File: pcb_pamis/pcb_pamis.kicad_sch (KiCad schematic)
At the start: 39 parts, among them J1 USB_C_Receptacle_USB2.0_16P, J10 Conn_01x03, J11 Conn_01x03, J12 Conn_02x06_Odd_Even, J2 1755736, J6 Conn_01x05, J7 Conn_01x05, J8 Conn_01x05, J9 Conn_01x03, Q1 Q_NPN_BEC, Q2 Q_NPN_BEC, SW1 SW_Push, U1 ESP32-WROOM-32UE, U2 CP2102N-Axx-xQFN28

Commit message: ajout fixations
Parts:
- added H1, H2, H3, H4: MountingHole_Pad, MountingHole:MountingHole_3.2mm_M3_ISO14580_Pad_TopBottom, symbol Mechanical:MountingHole_Pad
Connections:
- net GND: now also H1.1, H2.1, H3.1, H4.1

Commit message: commencement correctifs PCB Pami
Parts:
- H1, H2, H3, H4: footprint MountingHole:MountingHole_3.2mm_M3_ISO14580_Pad_TopBottom -> MountingHole:MountingHole_3.2mm_M3_Pad
- J10, J11, J9: footprint Connector_PinHeader_1.27mm:PinHeader_1x03_P1.27mm_Vertical -> Connector_PinHeader_2.54mm:PinHeader_1x03_P2.54mm_Vertical
- J12: footprint Connector_PinHeader_1.27mm:PinHeader_2x06_P1.27mm_Vertical -> Connector_PinHeader_2.54mm:PinHeader_2x06_P2.54mm_Vertical
- J6, J7, J8: footprint Connector_PinHeader_1.27mm:PinHeader_1x05_P1.27mm_Vertical -> Connector_PinHeader_2.54mm:PinHeader_1x05_P2.54mm_Vertical
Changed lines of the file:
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@@
 			)
 		)
-		(property "Footprint" "Connector_PinHeader_1.27mm:PinHeader_2x06_P1.27mm_Vertical"
+		(property "Footprint" "Connector_PinHeader_2.54mm:PinHeader_2x06_P2.54mm_Vertical"
 			(at 71.12 181.61 0)
 			(effects
@@
 			)
 		)
-		(property "Footprint" "Connector_PinHeader_1.27mm:PinHeader_1x03_P1.27mm_Vertical"
+		(property "Footprint" "Connector_PinHeader_2.54mm:PinHeader_1x03_P2.54mm_Vertical"
 			(at 100.33 80.01 0)
 			(effects
@@
 			)
 		)
-		(property "Footprint" "MountingHole:MountingHole_3.2mm_M3_ISO14580_Pad_TopBottom"
+		(property "Footprint" "MountingHole:MountingHole_3.2mm_M3_Pad"
 			(at 125.73 147.32 0)
 			(effects
@@
 			)
 		)
-		(property "Footprint" "Connector_PinHeader_1.27mm:PinHeader_1x05_P1.27mm_Vertical"
+		(property "Footprint" "Connector_PinHeader_2.54mm:PinHeader_1x05_P2.54mm_Vertical"
 			(at 81.28 111.76 0)
 			(effects
@@
 			)
 		)
-		(property "Footprint" "Connector_PinHeader_1.27mm:PinHeader_1x03_P1.27mm_Vertical"
+		(property "Footprint" "Connector_PinHeader_2.54mm:PinHeader_1x03_P2.54mm_Vertical"
 			(at 76.2 80.01 0)
 			(effects
@@
 			)
 		)
-		(property "Footprint" "Connector_PinHeader_1.27mm:PinHeader_1x03_P1.27mm_Vertical"
+		(property "Footprint" "Connector_PinHeader_2.54mm:PinHeader_1x03_P2.54mm_Vertical"
 			(at 125.73 80.01 0)
 			(effects
@@
 			)
 		)
-		(property "Footprint" "Connector_PinHeader_1.27mm:PinHeader_1x05_P1.27mm_Vertical"
+		(property "Footprint" "Connector_PinHeader_2.54mm:PinHeader_1x05_P2.54mm_Vertical"
 			(at 81.28 147.32 0)
 			(effects
@@
 			)
 		)
-		(property "Footprint" "MountingHole:MountingHole_3.2mm_M3_ISO14580_Pad_TopBottom"
+		(property "Footprint" "MountingHole:MountingHole_3.2mm_M3_Pad"
 			(at 140.97 147.32 0)
 			(effects
@@
 			)
 		)
-		(property "Footprint" "MountingHole:MountingHole_3.2mm_M3_ISO14580_Pad_TopBottom"
+		(property "Footprint" "MountingHole:MountingHole_3.2mm_M3_Pad"
 			(at 118.11 147.32 0)
 			(effects
@@
 			)
 		)
-		(property "Footprint" "MountingHole:MountingHole_3.2mm_M3_ISO14580_Pad_TopBottom"
+		(property "Footprint" "MountingHole:MountingHole_3.2mm_M3_Pad"
 			(at 133.35 147.32 0)
 			(effects
@@
 			)
 		)
-		(property "Footprint" "Connector_PinHeader_1.27mm:PinHeader_1x05_P1.27mm_Vertical"
+		(property "Footprint" "Connector_PinHeader_2.54mm:PinHeader_1x05_P2.54mm_Vertical"
 			(at 81.28 129.54 0)
 			(effects

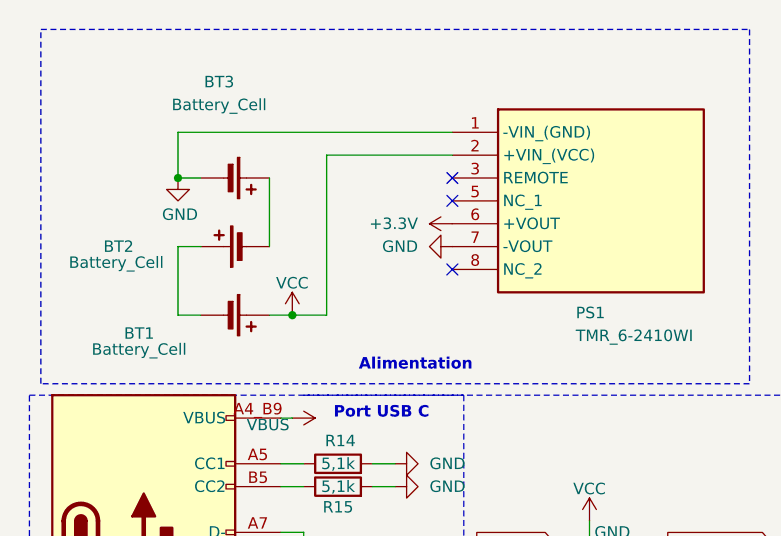
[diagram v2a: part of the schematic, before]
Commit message: finalisation nouveau routage
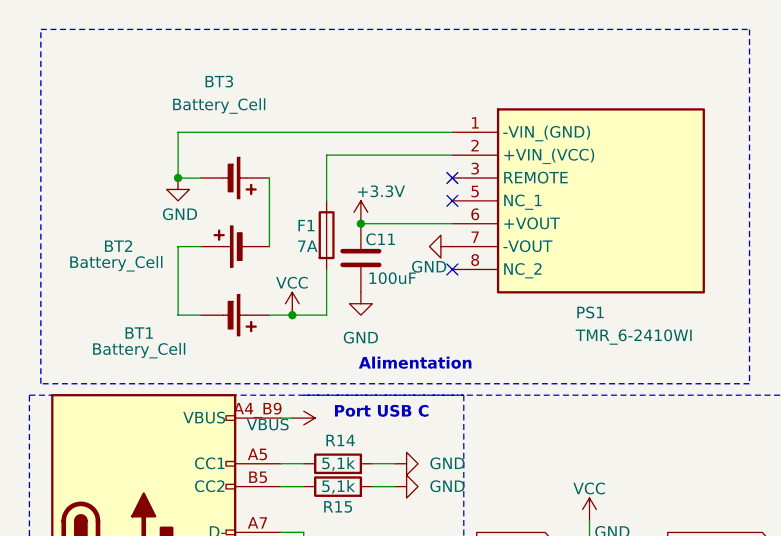
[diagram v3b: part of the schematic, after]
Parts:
- added C11: 100uF, Capacitor_SMD:C_1206_3216Metric_Pad1.33x1.80mm_HandSolder, symbol Device:C
- added F1: 7A, Modelec:01550900M, symbol Device:Fuse
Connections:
- net +3.3V: now also C11.1
- net GND: now also C11.2
- net VCC: now also F1.2; no longer PS1.2 (+VIN_(VCC))
- new net: F1.1, PS1.2 (+VIN_(VCC))
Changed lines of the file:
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@@
 	)
 	(junction
+		(at 50.8 35.56)
+		(diameter 0)
+		(color 0 0 0 0)
+	)
+	(junction
 		(at 182.88 149.86)
 		(diameter 0)
@@
 	(wire
 		(pts
-			(xy 265.43 19.05) (xy 265.43 22.86)
+			(xy 46.99 27.94) (xy 46.99 33.02)
 		)
 		(stroke
@@
 	(wire
 		(pts
-			(xy 165.1 33.02) (xy 163.83 33.02)
+			(xy 265.43 19.05) (xy 265.43 22.86)
 		)
 		(stroke
@@
 	(wire
 		(pts
-			(xy 46.99 45.72) (xy 46.99 27.94)
+			(xy 165.1 33.02) (xy 163.83 33.02)
 		)
 		(stroke
@@
 	(wire
 		(pts
+			(xy 50.8 35.56) (xy 60.96 35.56)
+		)
+		(stroke
+			(width 0)
+			(type default)
+		)
+	)
+	(wire
+		(pts
 			(xy 236.22 114.3) (xy 237.49 114.3)
 		)
@@
 		)
 	)
+	(wire
+		(pts
+			(xy 46.99 40.64) (xy 46.99 45.72)
+		)
+		(stroke
+			(width 0)
+			(type default)
+		)
+	)
 	(polyline
 		(pts
@@
 	(symbol
 		(lib_id "power:GND")
+		(at 50.8 43.18 0)
+		(unit 1)
+		(exclude_from_sim no)
+		(in_bom yes)
+		(on_board yes)
+		(dnp no)
+		(fields_autoplaced yes)
+		(property "Reference" "#PWR070"
+			(at 50.8 49.53 0)
+			(effects
+				(font
+					(size 1.27 1.27)
+				)
+				(hide yes)
+			)
+		)
+		(property "Value" "GND"
+			(at 50.8 48.26 0)
+			(effects
+				(font
+					(size 1.27 1.27)
+				)
+			)
+		)
+		(property "Footprint" ""
+			(at 50.8 43.18 0)
+			(effects
+				(font
+					(size 1.27 1.27)
+				)
+				(hide yes)
+			)
+		)
+		(property "Datasheet" ""
+			(at 50.8 43.18 0)
+			(effects
+				(font
+					(size 1.27 1.27)
+				)
+				(hide yes)
+			)
+		)
+		(property "Description" "Power symbol creates a global label with name \"GND\" , ground"
+			(at 50.8 43.18 0)
+			(effects
+				(font
+					(size 1.27 1.27)
+				)
+				(hide yes)
+			)
+		)
+		(pin "1"
+		)
+		(instances
+			(project ""
+				(path "/cd04cd30-6b87-4bc2-a277-438dac0065f3"
+					(reference "#PWR070")
+					(unit 1)
+				)
+			)
+		)
+	)
+	(symbol
+		(lib_id "power:GND")
 		(at 78.74 176.53 90)
 		(unit 1)
@@
 		(on_board yes)
 		(dnp no)
-		(fields_autoplaced yes)
 		(property "Reference" "#PWR02"
 			(at 54.61 38.1 0)
@@
 		)
 		(property "Value" "GND"
-			(at 57.15 38.0999 90)
+			(at 56.388 40.386 90)
 			(effects
 				(font
 					(size 1.27 1.27)
 				)
-				(justify right)
+				(justify left)
 			)
 		)
@@
 	)
 	(symbol
+		(lib_id "Device:Fuse")
+		(at 46.99 36.83 0)
+		(unit 1)
+		(exclude_from_sim no)
+		(in_bom yes)
+		(on_board yes)
+		(dnp no)
+		(property "Reference" "F1"
+			(at 43.688 35.814 0)
+			(effects
+				(font
+					(size 1.27 1.27)
+				)
+				(justify left)
+			)
+		)
+		(property "Value" "7A"
+			(at 43.688 38.1 0)
+			(effects
+				(font
+					(size 1.27 1.27)
+				)
+				(justify left)
+			)
+		)
+		(property "Footprint" "Modelec:01550900M"
+			(at 45.212 36.83 90)
+			(effects
+				(font
+					(size 1.27 1.27)
+				)
+				(hide yes)
+			)
+		)
+		(property "Datasheet" "~"
+			(at 46.99 36.83 0)
+			(effects
+				(font
+					(size 1.27 1.27)
+				)
+				(hide yes)
+			)
+		)
+		(property "Description" "Fuse"
+			(at 46.99 36.83 0)
+			(effects
+				(font
+					(size 1.27 1.27)
+				)
+				(hide yes)
+			)
+		)
+		(pin "2"
+		)
+		(pin "1"
+		)
+		(instances
+			(project ""
+				(path "/cd04cd30-6b87-4bc2-a277-438dac0065f3"
+					(reference "F1")
+					(unit 1)
+				)
+			)
+		)
+	)
+	(symbol
 		(lib_id "power:+3.3V")
 		(at 76.2 124.46 90)
@@
 	)
 	(symbol
+		(lib_id "Device:C")
+		(at 50.8 39.37 0)
+		(unit 1)
+		(exclude_from_sim no)
+		(in_bom yes)
+		(on_board yes)
+		(dnp no)
+		(property "Reference" "C11"
+			(at 51.308 37.338 0)
+			(effects
+				(font
+					(size 1.27 1.27)
+				)
+				(justify left)
+			)
+		)
+		(property "Value" "100uF"
+			(at 51.562 41.656 0)
+			(effects
+				(font
+					(size 1.27 1.27)
+				)
+				(justify left)
+			)
+		)
+		(property "Footprint" "Capacitor_SMD:C_1206_3216Metric_Pad1.33x1.80mm_HandSolder"
+			(at 51.7652 43.18 0)
+			(effects
+				(font
+					(size 1.27 1.27)
+				)
+				(hide yes)
+			)
+		)
+		(property "Datasheet" "~"
+			(at 50.8 39.37 0)
+			(effects
+				(font
+					(size 1.27 1.27)
+				)
+				(hide yes)
+			)
+		)
+		(property "Description" "Unpolarized capacitor"
+			(at 50.8 39.37 0)
+			(effects
+				(font
+					(size 1.27 1.27)
+				)
+				(hide yes)
+			)
+		)
+		(pin "2"
+		)
+		(pin "1"
+		)
+		(instances
+			(project ""
+				(path "/cd04cd30-6b87-4bc2-a277-438dac0065f3"
+					(reference "C11")
+					(unit 1)
+				)
+			)
+		)
+	)
+	(symbol
 		(lib_id "power:GND")
 		(at 128.27 74.93 180)
@@
 	(symbol
 		(lib_id "power:+3.3V")
-		(at 60.96 35.56 90)
+		(at 50.8 35.56 0)
 		(unit 1)
 		(exclude_from_sim no)
@@
 		(on_board yes)
 		(dnp no)
-		(fields_autoplaced yes)
 		(property "Reference" "#PWR01"
-			(at 64.77 35.56 0)
+			(at 50.8 39.37 0)
 			(effects
 				(font
@@
 		)
 		(property "Value" "+3.3V"
-			(at 57.15 35.5599 90)
+			(at 50.292 32.004 0)
 			(effects
 				(font
@@
 		)
 		(property "Footprint" ""
-			(at 60.96 35.56 0)
+			(at 50.8 35.56 0)
 			(effects
 				(font
@@
 		)
 		(property "Datasheet" ""
-			(at 60.96 35.56 0)
+			(at 50.8 35.56 0)
 			(effects
 				(font
@@
 		)
 		(property "Description" "Power symbol creates a global label with name \"+3.3V\""
-			(at 60.96 35.56 0)
+			(at 50.8 35.56 0)
 			(effects
 				(font

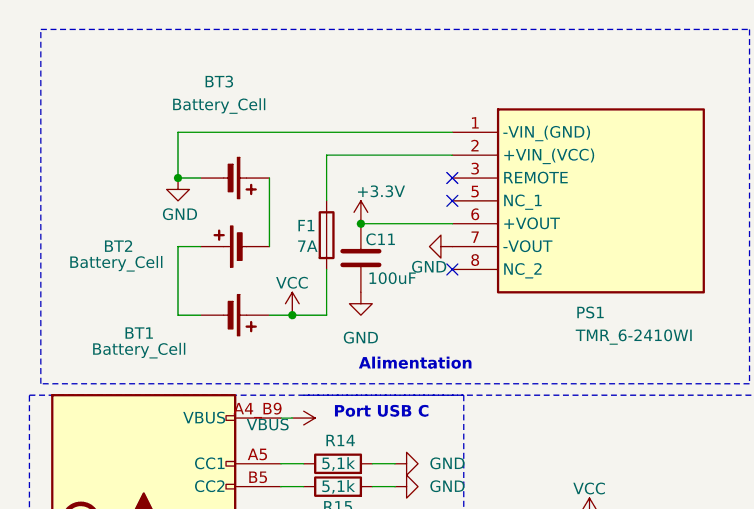
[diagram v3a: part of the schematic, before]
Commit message: déplacement fusible
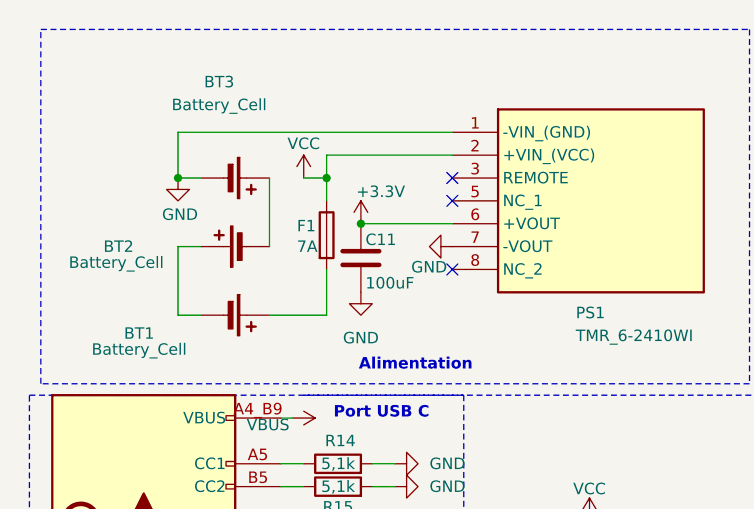
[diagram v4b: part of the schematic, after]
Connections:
- net VCC: now also F1.1, PS1.2 (+VIN_(VCC)); no longer BT1.P (+), F1.2
- new net: BT1.P (+), F1.2
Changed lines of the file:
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@@
 	)
 	(junction
-		(at 43.18 45.72)
-		(diameter 0)
-		(color 0 0 0 0)
-	)
-	(junction
 		(at 200.66 154.94)
 		(diameter 0)
@@
 	)
 	(junction
+		(at 46.99 30.48)
+		(diameter 0)
+		(color 0 0 0 0)
+	)
+	(junction
 		(at 25.4 120.65)
 		(diameter 0)
@@
 	(wire
 		(pts
+			(xy 44.45 30.48) (xy 46.99 30.48)
+		)
+		(stroke
+			(width 0)
+			(type default)
+		)
+	)
+	(wire
+		(pts
 			(xy 154.94 33.02) (xy 154.94 43.18)
 		)
@@
 	(wire
 		(pts
-			(xy 46.99 27.94) (xy 46.99 33.02)
+			(xy 46.99 30.48) (xy 46.99 33.02)
+		)
+		(stroke
+			(width 0)
+			(type default)
+		)
+	)
+	(wire
+		(pts
+			(xy 46.99 27.94) (xy 46.99 30.48)
 		)
 		(stroke
@@
 	(wire
 		(pts
-			(xy 43.18 45.72) (xy 40.64 45.72)
+			(xy 40.64 45.72) (xy 46.99 45.72)
 		)
 		(stroke
@@
 	(wire
 		(pts
-			(xy 43.18 45.72) (xy 46.99 45.72)
-		)
-		(stroke
-			(width 0)
-			(type default)
-		)
-	)
-	(wire
-		(pts
 			(xy 170.18 76.2) (xy 172.72 76.2)
 		)
@@
 	)
 	(symbol
-		(lib_id "power:VCC")
-		(at 43.18 45.72 0)
-		(unit 1)
-		(exclude_from_sim no)
-		(in_bom yes)
-		(on_board yes)
-		(dnp no)
-		(property "Reference" "#PWR032"
-			(at 43.18 49.53 0)
-			(effects
-				(font
-					(size 1.27 1.27)
-				)
-				(hide yes)
-			)
-		)
-		(property "Value" "VCC"
-			(at 43.18 42.164 0)
-			(effects
-				(font
-					(size 1.27 1.27)
-				)
-			)
-		)
-		(property "Footprint" ""
-			(at 43.18 45.72 0)
-			(effects
-				(font
-					(size 1.27 1.27)
-				)
-				(hide yes)
-			)
-		)
-		(property "Datasheet" ""
-			(at 43.18 45.72 0)
-			(effects
-				(font
-					(size 1.27 1.27)
-				)
-				(hide yes)
-			)
-		)
-		(property "Description" "Power symbol creates a global label with name \"VCC\""
-			(at 43.18 45.72 0)
-			(effects
-				(font
-					(size 1.27 1.27)
-				)
-				(hide yes)
-			)
-		)
-		(pin "1"
-		)
-		(instances
-			(project "pcb_pamis"
-				(path "/cd04cd30-6b87-4bc2-a277-438dac0065f3"
-					(reference "#PWR032")
-					(unit 1)
-				)
-			)
-		)
-	)
-	(symbol
 		(lib_id "power:GND")
 		(at 20.32 160.02 0)
@@
 	)
 	(symbol
+		(lib_id "power:VCC")
+		(at 44.45 30.48 0)
+		(unit 1)
+		(exclude_from_sim no)
+		(in_bom yes)
+		(on_board yes)
+		(dnp no)
+		(property "Reference" "#PWR032"
+			(at 44.45 34.29 0)
+			(effects
+				(font
+					(size 1.27 1.27)
+				)
+				(hide yes)
+			)
+		)
+		(property "Value" "VCC"
+			(at 44.45 26.67 0)
+			(effects
+				(font
+					(size 1.27 1.27)
+				)
+			)
+		)
+		(property "Footprint" ""
+			(at 44.45 30.48 0)
+			(effects
+				(font
+					(size 1.27 1.27)
+				)
+				(hide yes)
+			)
+		)
+		(property "Datasheet" ""
+			(at 44.45 30.48 0)
+			(effects
+				(font
+					(size 1.27 1.27)
+				)
+				(hide yes)
+			)
+		)
+		(property "Description" "Power symbol creates a global label with name \"VCC\""
+			(at 44.45 30.48 0)
+			(effects
+				(font
+					(size 1.27 1.27)
+				)
+				(hide yes)
+			)
+		)
+		(pin "1"
+		)
+		(instances
+			(project ""
+				(path "/cd04cd30-6b87-4bc2-a277-438dac0065f3"
+					(reference "#PWR032")
+					(unit 1)
+				)
+			)
+		)
+	)
+	(symbol
 		(lib_id "power:+3.3V")
 		(at 186.69 114.3 180)
@@
 		)
 		(property "Value" "100uF"
-			(at 51.562 41.656 0)
+			(at 51.308 42.164 0)
 			(effects
 				(font

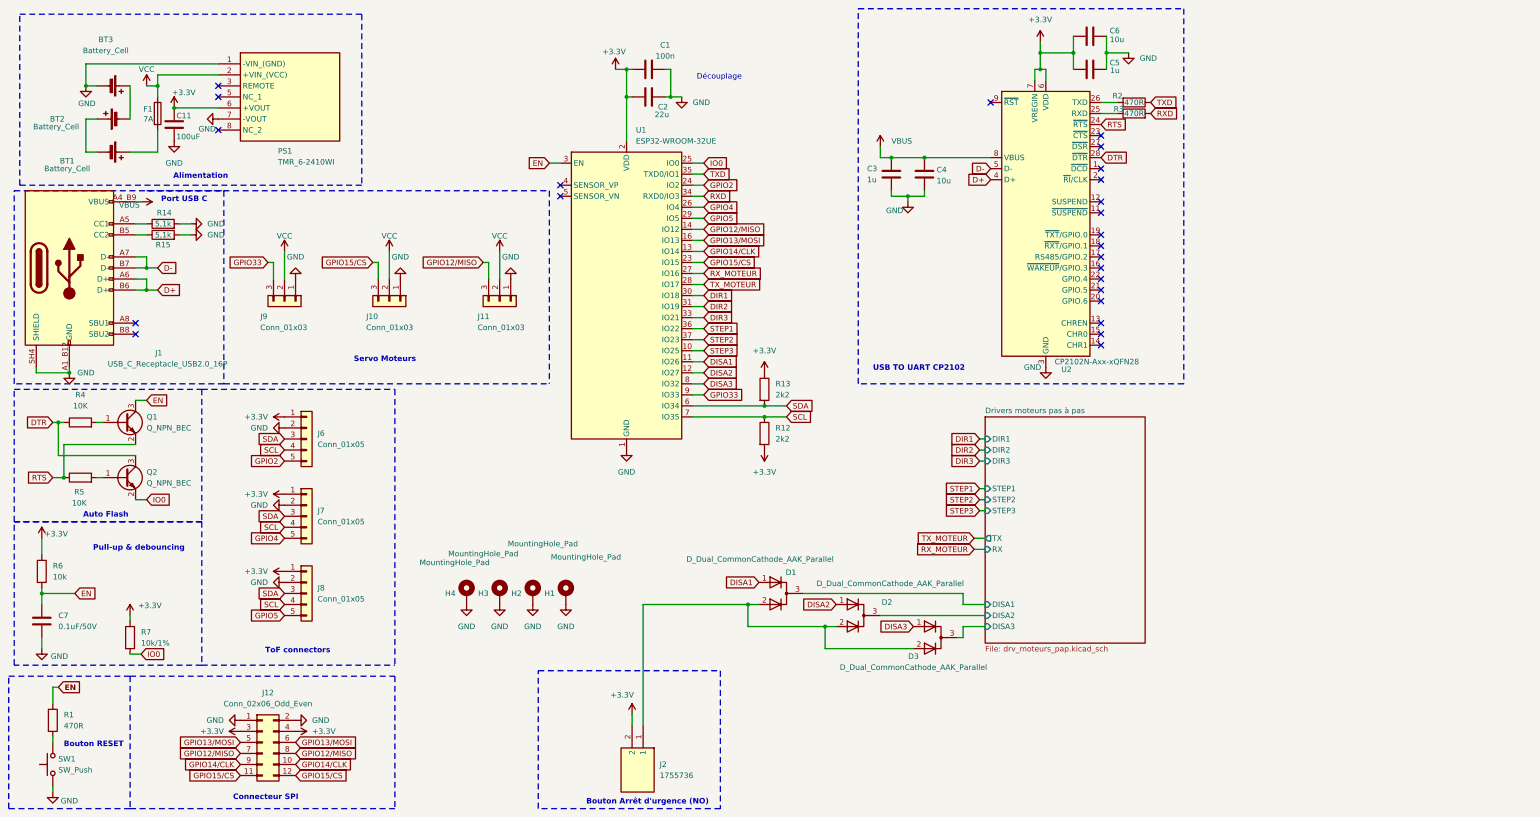
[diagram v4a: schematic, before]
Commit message: Ajout BAU servo PAMI, finitions PCB Actionneurs, fichier fab stencil. Version commandée PAMI & Actionneurs
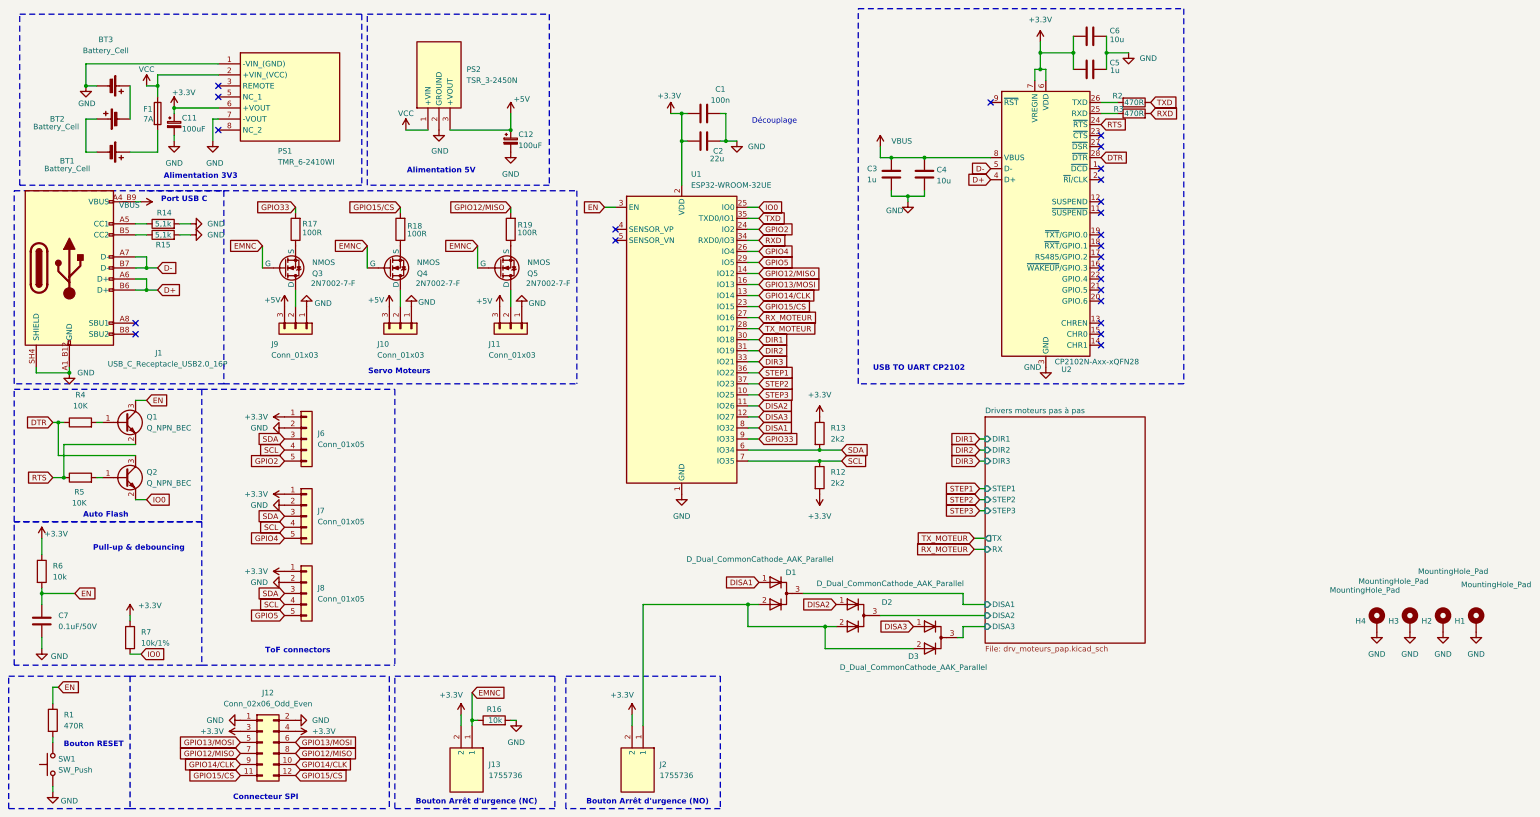
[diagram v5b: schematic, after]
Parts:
- removed C11: 100uF, Capacitor_SMD:C_1206_3216Metric_Pad1.33x1.80mm_HandSolder, symbol Device:C
- added C11, C12: 100uF, Capacitor_THT:C_Radial_D6.3mm_H11.0mm_P2.50mm, symbol Device:C_Polarized_Small
- added J13: 1755736, Modelec:PhoenixContact_MSTBVA_2,5_2-G-5,08_1x02_P5.08mm_Vertical, symbol Modelec:1755736
- added PS2: TSR_3-2450N, Modelec:TSR32450N, symbol Modelec:TSR_3-2450N
- added Q3, Q4, Q5: NMOS, Package_TO_SOT_SMD:SOT-23, symbol Simulation_SPICE:NMOS
- added R16: 10k, Resistor_SMD:R_0805_2012Metric_Pad1.20x1.40mm_HandSolder, symbol Device:R
- added R17, R18, R19: 100R, Resistor_SMD:R_0805_2012Metric_Pad1.20x1.40mm_HandSolder, symbol Device:R
- C2: footprint Capacitor_SMD:C_0805_2012Metric_Pad1.18x1.45mm_HandSolder -> Capacitor_SMD:C_1206_3216Metric_Pad1.33x1.80mm_HandSolder
- PS1: footprint TMR60510 -> Modelec:TMR60510
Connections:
- net +3.3V: now also C11.1, J13.2
- net DISA1: now also U1.8 (IO32); no longer U1.11 (IO26)
- net DISA2: now also U1.11 (IO26); no longer U1.12 (IO27)
- net DISA3: now also U1.12 (IO27); no longer U1.8 (IO32)
- net GND: now also C11.2, C12.2, PS2.2 (GROUND), R16.2
- net GPIO12/MISO: now also R19.2; no longer J11.3 (Pin_3)
- net GPIO15/CS: now also R18.2; no longer J10.3 (Pin_3)
- net GPIO33: now also R17.2; no longer J9.3 (Pin_3)
- net VCC: now also PS2.1 (+VIN); no longer J10.2 (Pin_2), J11.2 (Pin_2), J9.2 (Pin_2)
- new net: Q4.1 (S), R18.1
- new net: J10.2 (Pin_2), Q4.3 (D)
- new net: Q3.1 (S), R17.1
- new net: J9.2 (Pin_2), Q3.3 (D)
- new net: J11.2 (Pin_2), Q5.3 (D)
- new net: Q5.1 (S), R19.1
- new net +5V: C12.1, J10.3 (Pin_3), J11.3 (Pin_3), J9.3 (Pin_3), PS2.3 (+VOUT)
- new net EMNC: J13.1, Q3.2 (G), Q4.2 (G), Q5.2 (G), R16.1
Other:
- note added: "Alimentation 3V3"
- note added: "Alimentation 5V"
- note added: "Bouton Arrêt d'urgence (NC)"
- note removed: "Alimentation"
- moved on the sheet: C1, C2, H1, H2, H3, H4, J10, J11, J9, R12, R13, U1
